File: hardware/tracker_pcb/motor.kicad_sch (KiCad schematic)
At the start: 7 parts, among them IC2 DRV8244HQRYJRQ1

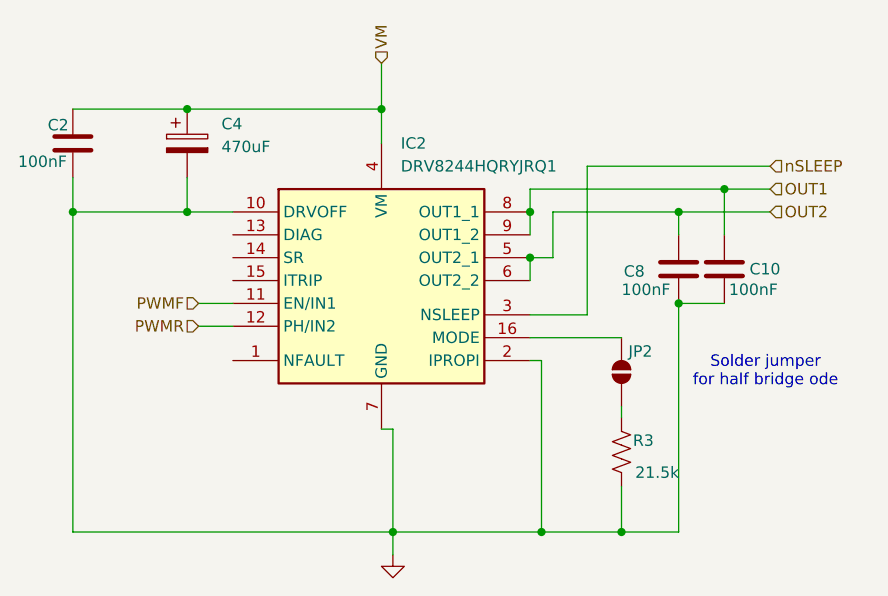
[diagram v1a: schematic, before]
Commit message: Complete but optos are using 5v pullups instead of 3v3.  No bueno
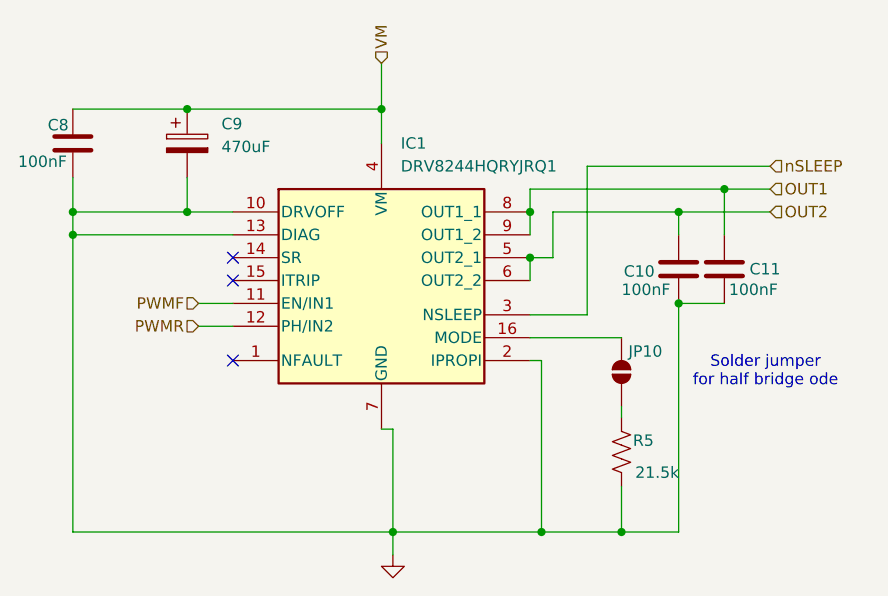
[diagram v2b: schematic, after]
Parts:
- IC1: renamed from IC2; footprint footprint:DRV8244HQRYJRQ1 -> RXZ0016A-MFG; symbol symbol:DRV8244HQRYJRQ1 -> symbol:DRV8245HQRXZRQ1
- renumbered C8 to C10, C10 to C11, C2 to C8, C4 to C9, JP2 to JP10, R3 to R5
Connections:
- net GND: now also IC1.13 (DIAG)
- no-connect marks 0 -> 3
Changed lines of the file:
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@@
+	)
+	(junction
+		(at 106.68 83.82)
+		(diameter 0)
+		(color 0 0 0 0)
 	)
 	(junction
@@
 	)
 	(junction
-		(at 106.68 83.82)
+		(at 157.48 83.82)
+		(diameter 0)
+		(color 0 0 0 0)
+	)
+	(junction
+		(at 106.68 86.36)
 		(diameter 0)
 		(color 0 0 0 0)
@@
 	)
 	(junction
-		(at 157.48 83.82)
-		(diameter 0)
-		(color 0 0 0 0)
-	)
-	(junction
 		(at 173.99 93.98)
 		(diameter 0)
@@
 		(color 0 0 0 0)
 	)
+	(no_connect
+		(at 124.46 88.9)
+	)
+	(no_connect
+		(at 124.46 100.33)
+	)
+	(no_connect
+		(at 124.46 91.44)
+	)
 	(wire
 		(pts
@@
 	(wire
 		(pts
+			(xy 157.48 83.82) (xy 157.48 86.36)
+		)
+		(stroke
+			(width 0)
+			(type default)
+		)
+	)
+	(wire
+		(pts
 			(xy 124.46 83.82) (xy 119.38 83.82)
 		)
@@
 	(wire
 		(pts
-			(xy 106.68 83.82) (xy 106.68 119.38)
+			(xy 106.68 83.82) (xy 106.68 86.36)
 		)
 		(stroke
@@
 	(wire
 		(pts
+			(xy 106.68 86.36) (xy 106.68 119.38)
+		)
+		(stroke
+			(width 0)
+			(type default)
+		)
+	)
+	(wire
+		(pts
 			(xy 179.07 81.28) (xy 157.48 81.28)
 		)
@@
 	(wire
 		(pts
+			(xy 106.68 86.36) (xy 124.46 86.36)
+		)
+		(stroke
+			(width 0)
+			(type default)
+		)
+	)
+	(wire
+		(pts
 			(xy 106.68 119.38) (xy 142.24 119.38)
 		)
@@
 		(pts
 			(xy 158.75 100.33) (xy 157.48 100.33)
-		)
-		(stroke
-			(width 0)
-			(type default)
-		)
-	)
-	(wire
-		(pts
-			(xy 157.48 83.82) (xy 157.48 86.36)
 		)
 		(stroke
@@
 		(on_board yes)
 		(dnp no)
-		(property "Reference" "R3"
+		(property "Reference" "R5"
 			(at 168.91 109.22 0)
 			(effects
@@
 			(project "tracker_pcb"
 				(path "/6aaa9514-f94e-4843-90d0-16960e4e49cb/7a9ac5e6-2be9-4d8c-8c5b-8ceb68264255"
-					(reference "R3")
+					(reference "R5")
 					(unit 1)
 				)
 				(path "/6aaa9514-f94e-4843-90d0-16960e4e49cb/f8a23924-a799-4920-a190-8ed5e6a03d20"
-					(reference "R1")
+					(reference "R6")
 					(unit 1)
 				)
@@
 		(dnp no)
 		(fields_autoplaced yes)
-		(property "Reference" "C4"
+		(property "Reference" "C9"
 			(at 123.19 74.0409 0)
 			(effects
@@
 			(project "tracker_pcb"
 				(path "/6aaa9514-f94e-4843-90d0-16960e4e49cb/7a9ac5e6-2be9-4d8c-8c5b-8ceb68264255"
-					(reference "C4")
+					(reference "C9")
 					(unit 1)
 				)
 				(path "/6aaa9514-f94e-4843-90d0-16960e4e49cb/f8a23924-a799-4920-a190-8ed5e6a03d20"
-					(reference "C3")
+					(reference "C13")
 					(unit 1)
 				)
@@
 		(on_board yes)
 		(dnp no)
-		(property "Reference" "C10"
+		(property "Reference" "C11"
 			(at 181.864 90.17 0)
 			(effects
@@
 			(project "tracker_pcb"
 				(path "/6aaa9514-f94e-4843-90d0-16960e4e49cb/7a9ac5e6-2be9-4d8c-8c5b-8ceb68264255"
-					(reference "C10")
+					(reference "C11")
 					(unit 1)
 				)
 				(path "/6aaa9514-f94e-4843-90d0-16960e4e49cb/f8a23924-a799-4920-a190-8ed5e6a03d20"
-					(reference "C6")
+					(reference "C15")
 					(unit 1)
 				)
@@
 		(dnp no)
 		(fields_autoplaced yes)
-		(property "Reference" "#PWR03"
+		(property "Reference" "#PWR011"
 			(at 142.24 128.27 0)
 			(effects
@@
 			(project "tracker_pcb"
 				(path "/6aaa9514-f94e-4843-90d0-16960e4e49cb/7a9ac5e6-2be9-4d8c-8c5b-8ceb68264255"
-					(reference "#PWR03")
+					(reference "#PWR011")
 					(unit 1)
 				)
 				(path "/6aaa9514-f94e-4843-90d0-16960e4e49cb/f8a23924-a799-4920-a190-8ed5e6a03d20"
-					(reference "#PWR06")
+					(reference "#PWR012")
 					(unit 1)
 				)
@@
 		(on_board yes)
 		(dnp no)
-		(property "Reference" "C8"
+		(property "Reference" "C10"
 			(at 167.894 90.424 0)
 			(effects
@@
 			(project "tracker_pcb"
 				(path "/6aaa9514-f94e-4843-90d0-16960e4e49cb/7a9ac5e6-2be9-4d8c-8c5b-8ceb68264255"
-					(reference "C8")
+					(reference "C10")
 					(unit 1)
 				)
 				(path "/6aaa9514-f94e-4843-90d0-16960e4e49cb/f8a23924-a799-4920-a190-8ed5e6a03d20"
-					(reference "C5")
+					(reference "C14")
 					(unit 1)
 				)
@@
 		(on_board yes)
 		(dnp no)
-		(property "Reference" "C2"
+		(property "Reference" "C8"
 			(at 103.886 74.168 0)
 			(effects
@@
 			(project "tracker_pcb"
 				(path "/6aaa9514-f94e-4843-90d0-16960e4e49cb/7a9ac5e6-2be9-4d8c-8c5b-8ceb68264255"
-					(reference "C2")
+					(reference "C8")
 					(unit 1)
 				)
 				(path "/6aaa9514-f94e-4843-90d0-16960e4e49cb/f8a23924-a799-4920-a190-8ed5e6a03d20"
-					(reference "C1")
+					(reference "C12")
 					(unit 1)
 				)
@@
 		(on_board yes)
 		(dnp no)
-		(property "Reference" "JP2"
+		(property "Reference" "JP10"
 			(at 168.402 99.314 90)
 			(effects
@@
 			(project "tracker_pcb"
 				(path "/6aaa9514-f94e-4843-90d0-16960e4e49cb/7a9ac5e6-2be9-4d8c-8c5b-8ceb68264255"
-					(reference "JP2")
+					(reference "JP10")
 					(unit 1)
 				)
 				(path "/6aaa9514-f94e-4843-90d0-16960e4e49cb/f8a23924-a799-4920-a190-8ed5e6a03d20"
-					(reference "JP1")
+					(reference "JP11")
 					(unit 1)
 				)
@@
 	)
 	(symbol
-		(lib_id "symbol:DRV8244HQRYJRQ1")
-		(at 124.46 83.82 0)
+		(lib_id "symbol:DRV8245HQRXZRQ1")
+		(at 137.16 130.81 0)
 		(unit 1)
 		(exclude_from_sim no)
@@
 		(dnp no)
 		(fields_autoplaced yes)
-		(property "Reference" "IC2"
+		(property "Reference" "IC1"
 			(at 143.1133 76.2 0)
 			(effects
@@
 			)
 		)
-		(property "Footprint" "footprint:DRV8244HQRYJRQ1"
-			(at 153.67 178.74 0)
+		(property "Footprint" "RXZ0016A-MFG"
+			(at 151.13 110.998 0)
+			(effects
+				(font
+					(size 1.27 1.27)
+					(italic yes)
+				)
+				(hide yes)
+			)
+		)
+		(property "Datasheet" "https://www.ti.com/lit/gpn/drv8245-q1"
+			(at 138.43 118.364 0)
+			(effects
+				(font
+					(size 1.27 1.27)
+					(italic yes)
+				)
+				(hide yes)
+			)
+		)
+		(property "Description" "Motor / Motion / Ignition Controllers & Drivers Automotive 40-V, 21-A H-Bridge driver with integrated current sensing and feedback 16-VQFN-HR -40 to 125"
+			(at 137.16 130.81 0)
+			(effects
+				(font
+					(size 1.27 1.27)
+				)
+				(hide yes)
+			)
+		)
+		(property "Height" ""
+			(at 166.37 525.73 0)
 			(effects
 				(font
@@
 			)
 		)
-		(property "Datasheet" "https://www.ti.com/lit/ds/symlink/drv8244-q1.pdf?ts=1695179222259&ref_url=https%253A%252F%252Fwww.ti.com%252Fproduct%252FDRV8244-Q1%253FkeyMatch%253DDRV8244-Q1%2526tisearch%253Dsearch-everything%2526usecase%253DGPN-ALT"
-			(at 153.67 278.74 0)
+		(property "Mouser Part Number" "595-DRV8244HQRYJRQ1"
+			(at 166.37 625.73 0)
 			(effects
 				(font
@@
 			)
 		)
-		(property "Description" "Motor / Motion / Ignition Controllers & Drivers Automotive 40-V, 21-A H-Bridge driver with integrated current sensing and feedback 16-VQFN-HR -40 to 125"
-			(at 124.46 83.82 0)
-			(effects
-				(font
-					(size 1.27 1.27)
-				)
-				(hide yes)
-			)
-		)
-		(property "Height" ""
-			(at 153.67 478.74 0)
+		(property "Mouser Price/Stock" "https://www.mouser.co.uk/ProductDetail/Texas-Instruments/DRV8244HQRYJRQ1?qs=Y0Uzf4wQF3nQ8wZEjQlEyg%3D%3D"
+			(at 166.37 725.73 0)
 			(effects
 				(font
@@
 			)
 		)
-		(property "Mouser Part Number" "595-DRV8244HQRYJRQ1"
-			(at 153.67 578.74 0)
+		(property "Manufacturer_Name" "Texas Instruments"
+			(at 166.37 825.73 0)
 			(effects
 				(font
@@
 			)
 		)
-		(property "Mouser Price/Stock" "https://www.mouser.co.uk/ProductDetail/Texas-Instruments/DRV8244HQRYJRQ1?qs=Y0Uzf4wQF3nQ8wZEjQlEyg%3D%3D"
-			(at 153.67 678.74 0)
-			(effects
-				(font
-					(size 1.27 1.27)
-				)
-				(justify left top)
-				(hide yes)
-			)
-		)
-		(property "Manufacturer_Name" "Texas Instruments"
-			(at 153.67 778.74 0)
-			(effects
-				(font
-					(size 1.27 1.27)
-				)
-				(justify left top)
-				(hide yes)
-			)
-		)
 		(property "Manufacturer_Part_Number" "DRV8244HQRYJRQ1"
-			(at 153.67 878.74 0)
+			(at 166.37 925.73 0)
 			(effects
 				(font
@@
 			(project "tracker_pcb"
 				(path "/6aaa9514-f94e-4843-90d0-16960e4e49cb/7a9ac5e6-2be9-4d8c-8c5b-8ceb68264255"
+					(reference "IC1")
+					(unit 1)
+				)
+				(path "/6aaa9514-f94e-4843-90d0-16960e4e49cb/f8a23924-a799-4920-a190-8ed5e6a03d20"
 					(reference "IC2")
 					(unit 1)
 				)
-				(path "/6aaa9514-f94e-4843-90d0-16960e4e49cb/f8a23924-a799-4920-a190-8ed5e6a03d20"
-					(reference "IC1")
-					(unit 1)
-				)

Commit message: WIP
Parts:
- removed JP10: SolderJumper_2_Open, Resistor_SMD:R_0402_1005Metric_Pad0.72x0.64mm_HandSolder, symbol Jumper:SolderJumper_2_Open
- added JP12: Jumper_2_Open, Connector_PinHeader_2.00mm:PinHeader_1x02_P2.00mm_Vertical, symbol Jumper:Jumper_2_Open
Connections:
- net at R5.2: now also JP12.2 (B)
- net at IC1.16 (MODE): now also JP12.1 (A)
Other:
- note added: "Install jumper for half bridge mode"
- note removed: "Solder jumper for half bridge ode"
- moved on the sheet: R5
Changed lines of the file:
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@@
 	(generator_version "9.0")
 	(paper "A4")
-	(text "Solder jumper\nfor half bridge ode"
+	(text "Install jumper\nfor half bridge mode"
 		(exclude_from_sim no)
 		(at 183.642 101.6 0)
@@
 	(wire
 		(pts
-			(xy 167.64 114.3) (xy 167.64 119.38)
+			(xy 167.64 116.84) (xy 167.64 119.38)
 		)
 		(stroke
@@
 	(wire
 		(pts
-			(xy 167.64 106.68) (xy 167.64 105.41)
+			(xy 167.64 97.79) (xy 167.64 99.06)
 		)
 		(stroke
@@
 	(symbol
 		(lib_id "Device:R_US")
-		(at 167.64 110.49 180)
+		(at 167.64 113.03 180)
 		(unit 1)
 		(exclude_from_sim no)
@@
 		(dnp no)
 		(property "Reference" "R5"
-			(at 168.91 109.22 0)
+			(at 168.91 111.76 0)
 			(effects
 				(font
@@
 		)
 		(property "Value" "21.5k"
-			(at 169.164 112.776 0)
+			(at 169.164 115.316 0)
 			(effects
 				(font
@@
 		)
 		(property "Footprint" "Resistor_SMD:R_0603_1608Metric"
-			(at 166.624 110.236 90)
+			(at 166.624 112.776 90)
 			(effects
 				(font
@@
 		)
 		(property "Datasheet" "~"
-			(at 167.64 110.49 0)
+			(at 167.64 113.03 0)
 			(effects
 				(font
@@
 		)
 		(property "Description" "Resistor, US symbol"
-			(at 167.64 110.49 0)
+			(at 167.64 113.03 0)
 			(effects
 				(font
@@
 	)
 	(symbol
+		(lib_id "Jumper:Jumper_2_Open")
+		(at 167.64 104.14 270)
+		(unit 1)
+		(exclude_from_sim no)
+		(in_bom yes)
+		(on_board yes)
+		(dnp no)
+		(property "Reference" "JP12"
+			(at 170.942 104.394 0)
+			(effects
+				(font
+					(size 1.27 1.27)
+				)
+			)
+		)
+		(property "Value" "Jumper_2_Open"
+			(at 165.354 104.394 0)
+			(effects
+				(font
+					(size 1.27 1.27)
+				)
+				(hide yes)
+			)
+		)
+		(property "Footprint" "Connector_PinHeader_2.00mm:PinHeader_1x02_P2.00mm_Vertical"
+			(at 167.64 104.14 0)
+			(effects
+				(font
+					(size 1.27 1.27)
+				)
+				(hide yes)
+			)
+		)
+		(property "Datasheet" "~"
+			(at 167.64 104.14 0)
+			(effects
+				(font
+					(size 1.27 1.27)
+				)
+				(hide yes)
+			)
+		)
+		(property "Description" "Jumper, 2-pole, open"
+			(at 167.64 104.14 0)
+			(effects
+				(font
+					(size 1.27 1.27)
+				)
+				(hide yes)
+			)
+		)
+		(pin "2"
+		)
+		(pin "1"
+		)
+		(instances
+			(project "tracker_pcb"
+				(path "/6aaa9514-f94e-4843-90d0-16960e4e49cb/7a9ac5e6-2be9-4d8c-8c5b-8ceb68264255"
+					(reference "JP12")
+					(unit 1)
+				)
+				(path "/6aaa9514-f94e-4843-90d0-16960e4e49cb/f8a23924-a799-4920-a190-8ed5e6a03d20"
+					(reference "JP13")
+					(unit 1)
+				)
+			)
+		)
+	)
+	(symbol
 		(lib_id "Device:C")
 		(at 179.07 90.17 0)
@@
 					(unit 1)
 				)
-			)
-		)
-	)
-	(symbol
-		(lib_id "Jumper:SolderJumper_2_Open")
-		(at 167.64 101.6 90)
-		(unit 1)
-		(exclude_from_sim no)
-		(in_bom no)
-		(on_board yes)
-		(dnp no)
-		(property "Reference" "JP10"
-			(at 168.402 99.314 90)
-			(effects
-				(font
-					(size 1.27 1.27)
-				)
-				(justify right)
-			)
-		)
-		(property "Value" "SolderJumper_2_Open"
-			(at 163.83 101.6 0)
-			(effects
-				(font
-					(size 1.27 1.27)
-				)
-				(hide yes)
-			)
-		)
-		(property "Footprint" "Resistor_SMD:R_0402_1005Metric_Pad0.72x0.64mm_HandSolder"
-			(at 167.64 101.6 0)
-			(effects
-				(font
-					(size 1.27 1.27)
-				)
-				(hide yes)
-			)
-		)
-		(property "Datasheet" "~"
-			(at 167.64 101.6 0)
-			(effects
-				(font
-					(size 1.27 1.27)
-				)
-				(hide yes)
-			)
-		)
-		(property "Description" "Solder Jumper, 2-pole, open"
-			(at 167.64 101.6 0)
-			(effects
-				(font
-					(size 1.27 1.27)
-				)
-				(hide yes)
-			)
-		)
-		(pin "2"
-		)
-		(pin "1"
-		)
-		(instances
-			(project "tracker_pcb"
-				(path "/6aaa9514-f94e-4843-90d0-16960e4e49cb/7a9ac5e6-2be9-4d8c-8c5b-8ceb68264255"
-					(reference "JP10")
-					(unit 1)
-				)
-				(path "/6aaa9514-f94e-4843-90d0-16960e4e49cb/f8a23924-a799-4920-a190-8ed5e6a03d20"
-					(reference "JP11")
-					(unit 1)
-				)

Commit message: Including LORA wio-sx1262
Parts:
- removed IC1: DRV8244HQRYJRQ1, RXZ0016A-MFG, symbol symbol:DRV8245HQRXZRQ1
- removed JP12: Jumper_2_Open, Connector_PinHeader_2.00mm:PinHeader_1x02_P2.00mm_Vertical, symbol Jumper:Jumper_2_Open
- removed R5: 21.5k, Resistor_SMD:R_0603_1608Metric, symbol Device:R_US
- added C22: 100nF, Capacitor_SMD:C_0603_1608Metric, symbol Device:C
- added IC1: DRV8244SQRYJRQ1, footprint:DRV8244HQRYJRQ1, symbol symbol:DRV8244SQRYJRQ1
- added R7: 780R, Resistor_SMD:R_0603_1608Metric, symbol Device:R_US
- C10: renamed from C8; LCSC (none) -> C1590
- C11: renamed from C9; LCSC (none) -> C688951
- C12: renamed from C10; LCSC (none) -> C1590
- C13: renamed from C11; LCSC (none) -> C1590
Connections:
- net GND: now also C22.2, IC1.10 (DRVOFF), IC1.7 (GND), R7.1
- net OUT1: now also IC1.8 (OUT1_1), IC1.9 (OUT1_2)
- net OUT2: now also IC1.5 (OUT2_1), IC1.6 (OUT2_2)
- net PWMF: now also IC1.11 (EN/IN1)
- net PWMR: now also IC1.12 (PH/IN2)
- net VM: now also IC1.3 (NSLEEP), IC1.4 (VM)
- new net IOUT: C22.1, IC1.2 (IPROPI), R7.2
- new net SCLK: IC1.14 (SCLK)
- new net SDI: IC1.15 (SDI)
- new net SDO: IC1.16 (SDO)
- new net nSCS: IC1.13 (nSCS)
- no-connect marks 3 -> 1
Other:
- note removed: "Install jumper for half bridge mode"
- moved on the sheet: C10, C11, C12, C13

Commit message: VIA changes
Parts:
- R7: value 780R -> 820R; LCSC (none) -> C23253
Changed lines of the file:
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@@
 			)
 		)
-		(property "Value" "780R"
+		(property "Value" "820R"
 			(at 223.774 65.786 0)
 			(effects
@@
 			(effects
 				(font
+					(size 1.27 1.27)
+				)
+				(hide yes)
+			)
+		)
+		(property "LCSC" "C23253"
+			(at 223.774 64.008 0)
+			(effects
+				(font

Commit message: ss changes
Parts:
- removed C22: 100nF, Capacitor_SMD:C_0603_1608Metric, symbol Device:C
- removed R7: 820R, Resistor_SMD:R_0603_1608Metric, symbol Device:R_US
- IC1: footprint footprint:DRV8244HQRYJRQ1 -> DRV8244HQRYJRQ1
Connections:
- net IOUT is gone; now on net GND: IC1.2 (IPROPI)
- net ~{nFAULT}: now reaches IC1.1 (~{nFAULT})
- net nSCS renamed ~{nSCS}
- no-connect marks 1 -> 0
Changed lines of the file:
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@@
-	)
-	(junction
-		(at 229.87 57.15)
-		(diameter 0)
-		(color 0 0 0 0)
 	)
 	(junction
@@
 	)
 	(junction
-		(at 234.95 57.15)
-		(diameter 0)
-		(color 0 0 0 0)
-	)
-	(junction
 		(at 213.36 29.21)
 		(diameter 0)
@@
 	)
 	(junction
-		(at 234.95 72.39)
-		(diameter 0)
-		(color 0 0 0 0)
-	)
-	(junction
 		(at 241.3 72.39)
 		(diameter 0)
 		(color 0 0 0 0)
 	)
-	(no_connect
-		(at 229.87 52.07)
-	)
 	(wire
 		(pts
@@
 	(wire
 		(pts
+			(xy 229.87 57.15) (xy 229.87 72.39)
+		)
+		(stroke
+			(width 0)
+			(type default)
+		)
+	)
+	(wire
+		(pts
 			(xy 246.38 49.53) (xy 246.38 72.39)
 		)
@@
 	(wire
 		(pts
-			(xy 234.95 57.15) (xy 236.22 57.15)
-		)
-		(stroke
-			(width 0)
-			(type default)
-		)
-	)
-	(wire
-		(pts
-			(xy 229.87 57.15) (xy 229.87 60.96)
-		)
-		(stroke
-			(width 0)
-			(type default)
-		)
-	)
-	(wire
-		(pts
 			(xy 246.38 72.39) (xy 251.46 72.39)
 		)
@@
 	(wire
 		(pts
-			(xy 229.87 68.58) (xy 229.87 72.39)
-		)
-		(stroke
-			(width 0)
-			(type default)
-		)
-	)
-	(wire
-		(pts
 			(xy 251.46 49.53) (xy 251.46 72.39)
 		)
@@
 	(wire
 		(pts
-			(xy 234.95 72.39) (xy 229.87 72.39)
-		)
-		(stroke
-			(width 0)
-			(type default)
-		)
-	)
-	(wire
-		(pts
 			(xy 166.37 29.21) (xy 173.99 29.21)
 		)
@@
 	(wire
 		(pts
-			(xy 234.95 57.15) (xy 234.95 60.96)
-		)
-		(stroke
-			(width 0)
-			(type default)
-		)
-	)
-	(wire
-		(pts
 			(xy 194.31 41.91) (xy 196.85 41.91)
 		)
@@
 	(wire
 		(pts
+			(xy 229.87 52.07) (xy 256.54 52.07)
+		)
+		(stroke
+			(width 0)
+			(type default)
+		)
+	)
+	(wire
+		(pts
 			(xy 229.87 72.39) (xy 213.36 72.39)
 		)
@@
 	(wire
 		(pts
-			(xy 229.87 57.15) (xy 234.95 57.15)
-		)
-		(stroke
-			(width 0)
-			(type default)
-		)
-	)
-	(wire
-		(pts
 			(xy 194.31 46.99) (xy 196.85 46.99)
 		)
@@
 	(wire
 		(pts
-			(xy 234.95 68.58) (xy 234.95 72.39)
-		)
-		(stroke
-			(width 0)
-			(type default)
-		)
-	)
-	(wire
-		(pts
 			(xy 182.88 55.88) (xy 196.85 55.88)
 		)
@@
 	(wire
 		(pts
-			(xy 241.3 72.39) (xy 234.95 72.39)
+			(xy 229.87 72.39) (xy 241.3 72.39)
 		)
 		(stroke
@@
 		)
 	)
-	(hierarchical_label "IOUT"
-		(shape input)
-		(at 236.22 57.15 90)
-		(effects
-			(font
-				(size 1.27 1.27)
-			)
-			(justify left)
-		)
-	)
-	(hierarchical_label "nSCS"
+	(hierarchical_label "~{nSCS}"
 		(shape input)
 		(at 194.31 39.37 180)
@@
 		(shape input)
 		(at 256.54 36.83 0)
+		(effects
+			(font
+				(size 1.27 1.27)
+			)
+			(justify left)
+		)
+	)
+	(hierarchical_label "~{nFAULT}"
+		(shape input)
+		(at 256.54 52.07 0)
 		(effects
 			(font
@@
 			)
 		)
-		(property "Footprint" "footprint:DRV8244HQRYJRQ1"
+		(property "Footprint" "DRV8244HQRYJRQ1"
 			(at 226.06 134.29 0)
 			(effects
@@
 					(unit 1)
 				)
-			)
-		)
-	)
-	(symbol
-		(lib_id "Device:R_US")
-		(at 229.87 64.77 180)
-		(unit 1)
-		(exclude_from_sim no)
-		(in_bom yes)
-		(on_board yes)
-		(dnp no)
-		(property "Reference" "R7"
-			(at 223.774 64.008 0)
-			(effects
-				(font
-					(size 1.27 1.27)
-				)
-				(justify right)
-			)
-		)
-		(property "Value" "820R"
-			(at 223.774 65.786 0)
-			(effects
-				(font
-					(size 1.27 1.27)
-				)
-				(justify right)
-			)
-		)
-		(property "Footprint" "Resistor_SMD:R_0603_1608Metric"
-			(at 228.854 64.516 90)
-			(effects
-				(font
-					(size 1.27 1.27)
-				)
-				(hide yes)
-			)
-		)
-		(property "Datasheet" "~"
-			(at 229.87 64.77 0)
-			(effects
-				(font
-					(size 1.27 1.27)
-				)
-				(hide yes)
-			)
-		)
-		(property "Description" "Resistor, US symbol"
-			(at 229.87 64.77 0)
-			(effects
-				(font
-					(size 1.27 1.27)
-				)
-				(hide yes)
-			)
-		)
-		(property "LCSC" "C23253"
-			(at 223.774 64.008 0)
-			(effects
-				(font
-					(size 1.27 1.27)
-				)
-				(hide yes)
-			)
-		)
-		(pin "1"
-		)
-		(pin "2"
-		)
-		(instances
-			(project "tracker_pcb"
-				(path "/6aaa9514-f94e-4843-90d0-16960e4e49cb/7a9ac5e6-2be9-4d8c-8c5b-8ceb68264255"
-					(reference "R7")
-					(unit 1)
-				)
-				(path "/6aaa9514-f94e-4843-90d0-16960e4e49cb/f8a23924-a799-4920-a190-8ed5e6a03d20"
-					(reference "R8")
-					(unit 1)
-				)
-			)
-		)
-	)
-	(symbol
-		(lib_id "Device:C")
-		(at 234.95 64.77 0)
-		(unit 1)
-		(exclude_from_sim no)
-		(in_bom yes)
-		(on_board yes)
-		(dnp no)
-		(property "Reference" "C22"
-			(at 235.204 62.738 0)
-			(effects
-				(font
-					(size 1.27 1.27)
-				)
-				(justify left)
-			)
-		)
-		(property "Value" "100nF"
-			(at 235.458 67.056 0)
-			(effects
-				(font
-					(size 1.27 1.27)
-				)
-				(justify left)
-			)
-		)
-		(property "Footprint" "Capacitor_SMD:C_0603_1608Metric"
-			(at 235.9152 68.58 0)
-			(effects
-				(font
-					(size 1.27 1.27)
-				)
-				(hide yes)
-			)
-		)
-		(property "Datasheet" "~"
-			(at 234.95 64.77 0)
-			(effects
-				(font
-					(size 1.27 1.27)
-				)
-				(hide yes)
-			)
-		)
-		(property "Description" "Unpolarized capacitor"
-			(at 234.95 64.77 0)
-			(effects
-				(font
-					(size 1.27 1.27)
-				)
-				(hide yes)
-			)
-		)
-		(property "LCSC" "C1590"
-			(at 235.204 62.738 0)
-			(effects
-				(font
-					(size 1.27 1.27)
-				)
-				(hide yes)
-			)
-		)
-		(pin "2"
-		)
-		(pin "1"
-		)
-		(instances
-			(project "tracker_pcb"
-				(path "/6aaa9514-f94e-4843-90d0-16960e4e49cb/7a9ac5e6-2be9-4d8c-8c5b-8ceb68264255"
-					(reference "C22")
-					(unit 1)
-				)
-				(path "/6aaa9514-f94e-4843-90d0-16960e4e49cb/f8a23924-a799-4920-a190-8ed5e6a03d20"
-					(reference "C23")
-					(unit 1)
-				)
